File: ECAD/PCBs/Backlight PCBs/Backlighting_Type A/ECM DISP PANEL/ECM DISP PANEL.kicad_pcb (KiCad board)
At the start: 2 copper layers, 110.3 x 171.8 mm, 91 parts, among them J1 BL IN, J2 BL OUT, J3 ECM JETT, SW1 ECM JETT

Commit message: Drawing Sheet & Silkscreen update - Backlight Panels(An - Fc)
1:  Updated/Relinked Drawing Sheet for both PCB and Schematics
2:  Standardized Silkscreen (if required)
3:  Added WS2812B symbol to OH Library (for future schematic fixing)

ANT SEL thru FCS PANEL
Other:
- board text added: "ECM DISP PANEL Revision: 3 www.openhornet.com"
- board text removed: "DISP-EMC Panel Backlight Designed by L. Walker"
- board text removed: "Version 2.6"
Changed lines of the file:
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@@
   )
   (paper "A4")
+  (title_block
+    (title "ECM DISP PANEL")
+    (date "2023-02-10")
+    (rev "3")
+  )
   (layers
     (0 "F.Cu" signal)
@@
     (effects (font (size 1 1) (thickness 0.15)) (justify mirror))
   )
-  (gr_text "DISP-EMC Panel Backlight\nDesigned by L. Walker" (at 131.318 119.38) (layer "B.SilkS")
-    (effects (font (size 1 1) (thickness 0.15)) (justify left mirror))
-  )
-  (gr_text "Version 2.6" (at 87.884 117.348) (layer "B.SilkS")
+  (gr_text "ECM DISP PANEL\nRevision: 3\nwww.openhornet.com" (at 125.779172 119.871122) (layer "B.SilkS")
     (effects (font (size 1 1) (thickness 0.15)) (justify mirror))
   )

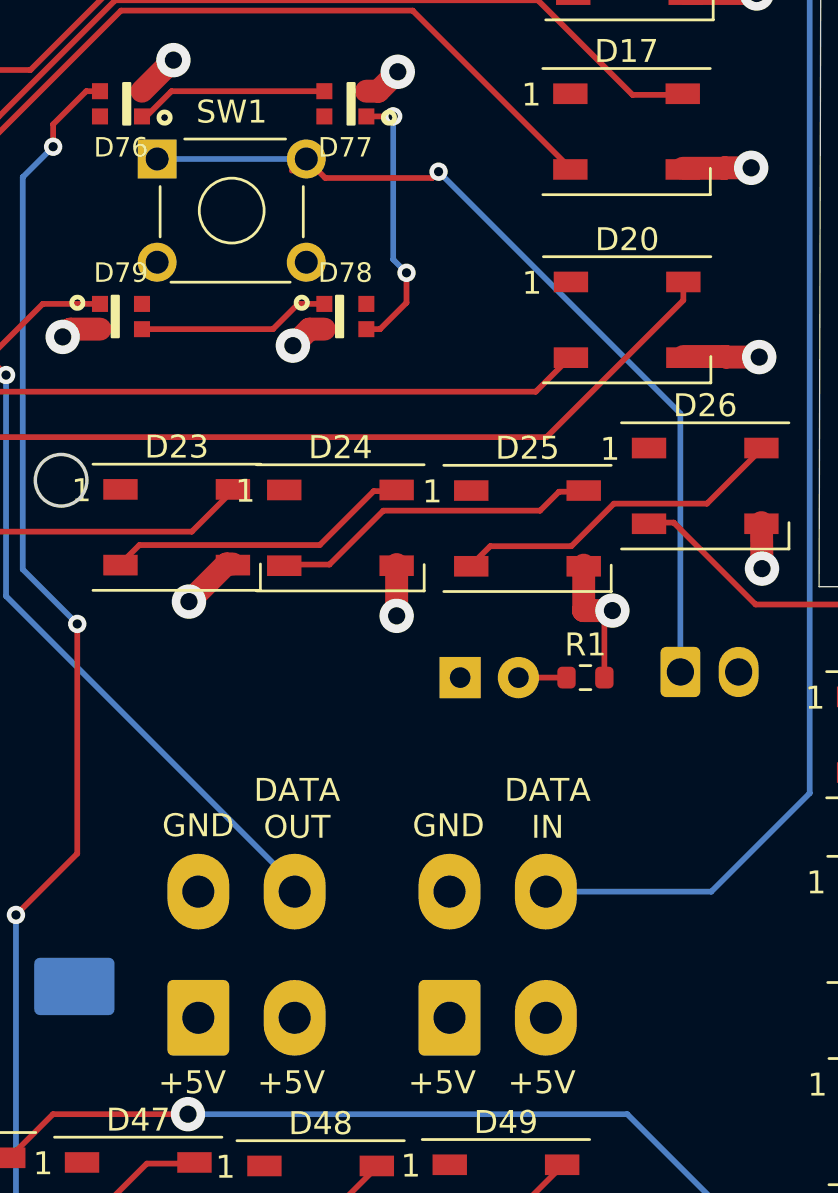
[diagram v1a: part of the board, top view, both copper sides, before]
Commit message: Review: COMM thru ECM DISP 100%
COMM PANEL
DEFOG PANEL
ECM DISP PANEL

Reviewed/adjusted silkscreens as needed
Adjusted values of footprints
Relinked footprints
Updated Manufacturing files
Updated PNGs and STEP files as needed.
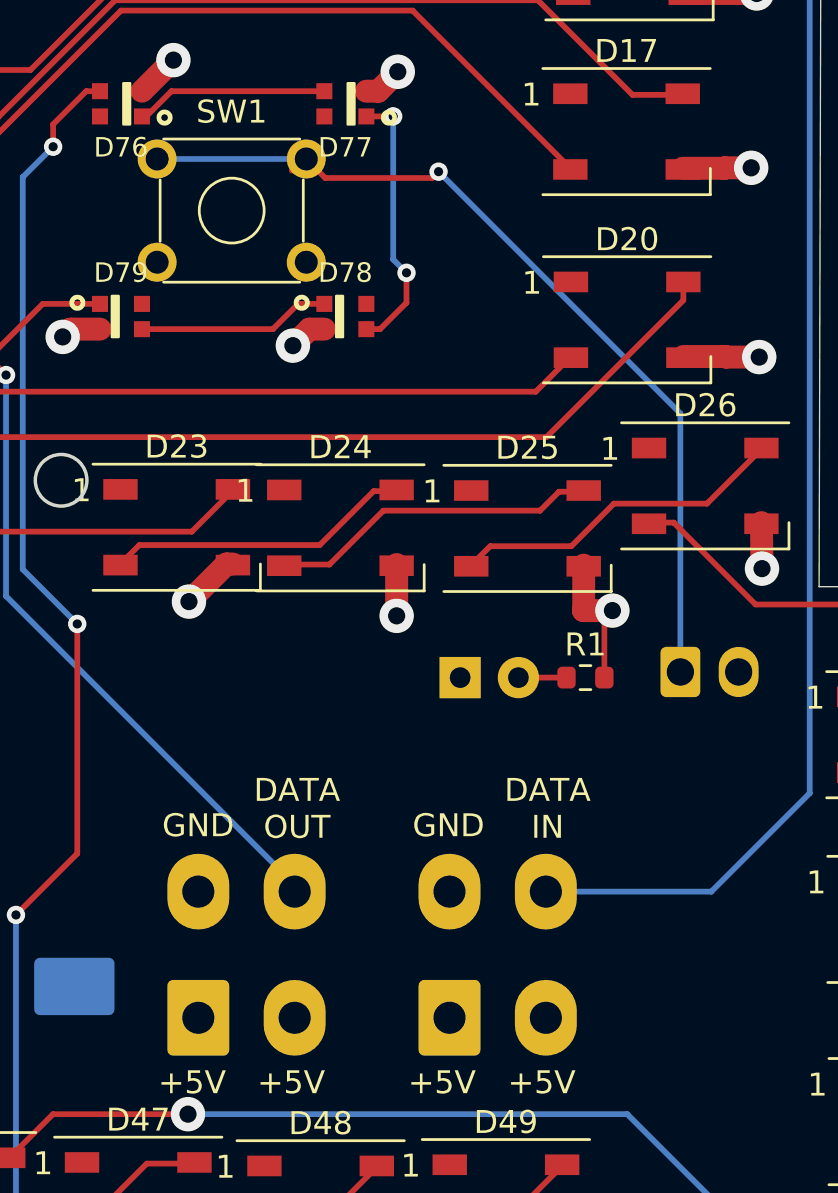
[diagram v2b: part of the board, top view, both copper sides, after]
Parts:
- C1: value 1000 nF -> 1000uF (C_Polarized)
- D1: value READY -> LED
- D76, D77, D78, D79: value LED -> REF**
- H1, H2, H3, H4, H5, H6: footprint MountingHole:MountingHole_4.5mm -> OH_Footprints:MountingHole_4.5mm
- R1: value R -> 470

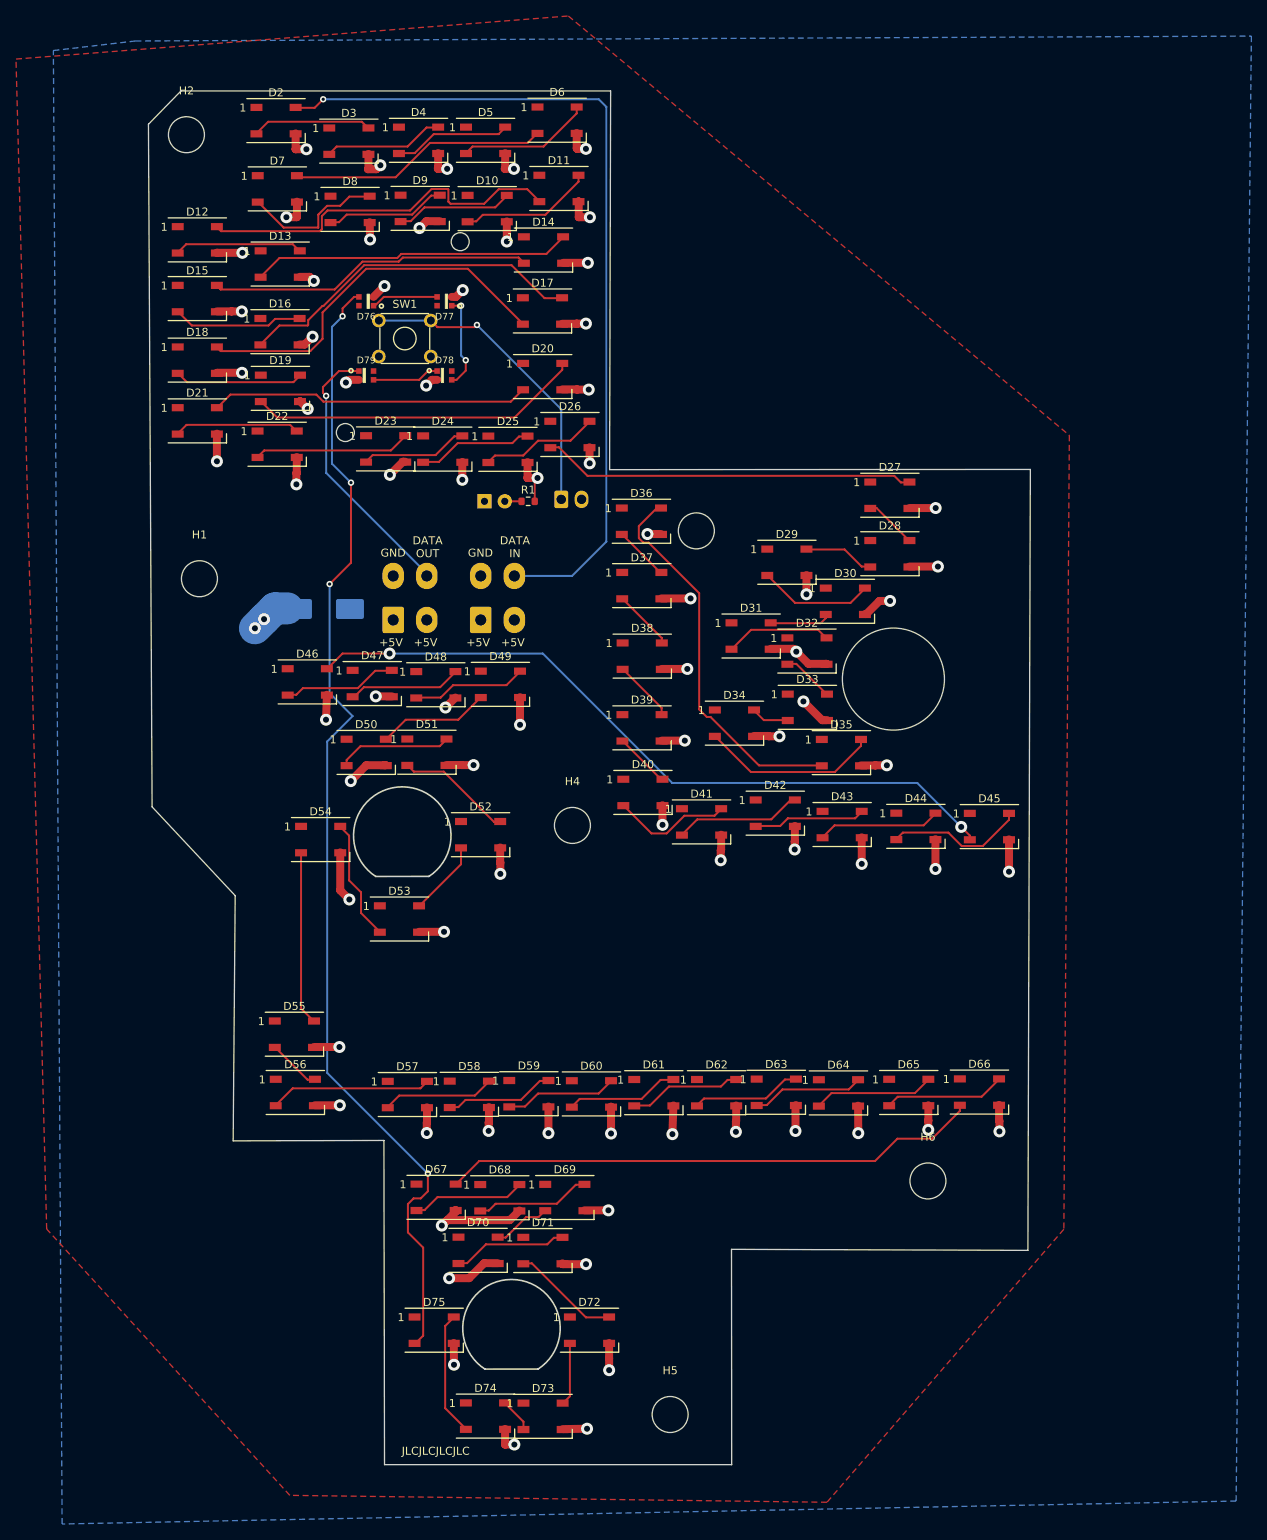
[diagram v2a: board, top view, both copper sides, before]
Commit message: Kicad 7 Transition - ECM DISP PANEL
Added 3d model and updated footprint/symbol properties for Tactical Switch, Omron B3F-1026 -
Added footprint/symbol for #0-80 mounting hole
Updated WS2818B-2020 footprint
Updated custom design rules for panels (ANT SEL thru DEFOG)

ECM DISP PANEL:
Consolidated BOM.
Updated manufacturing files
Fixed PCB routing - removed unneeded vias/traces
Fixed clearance issues around NPTHs
Updated WS2818B-2020
Schematic/PCB standardization
Updated Assets (PNGs, STEP)
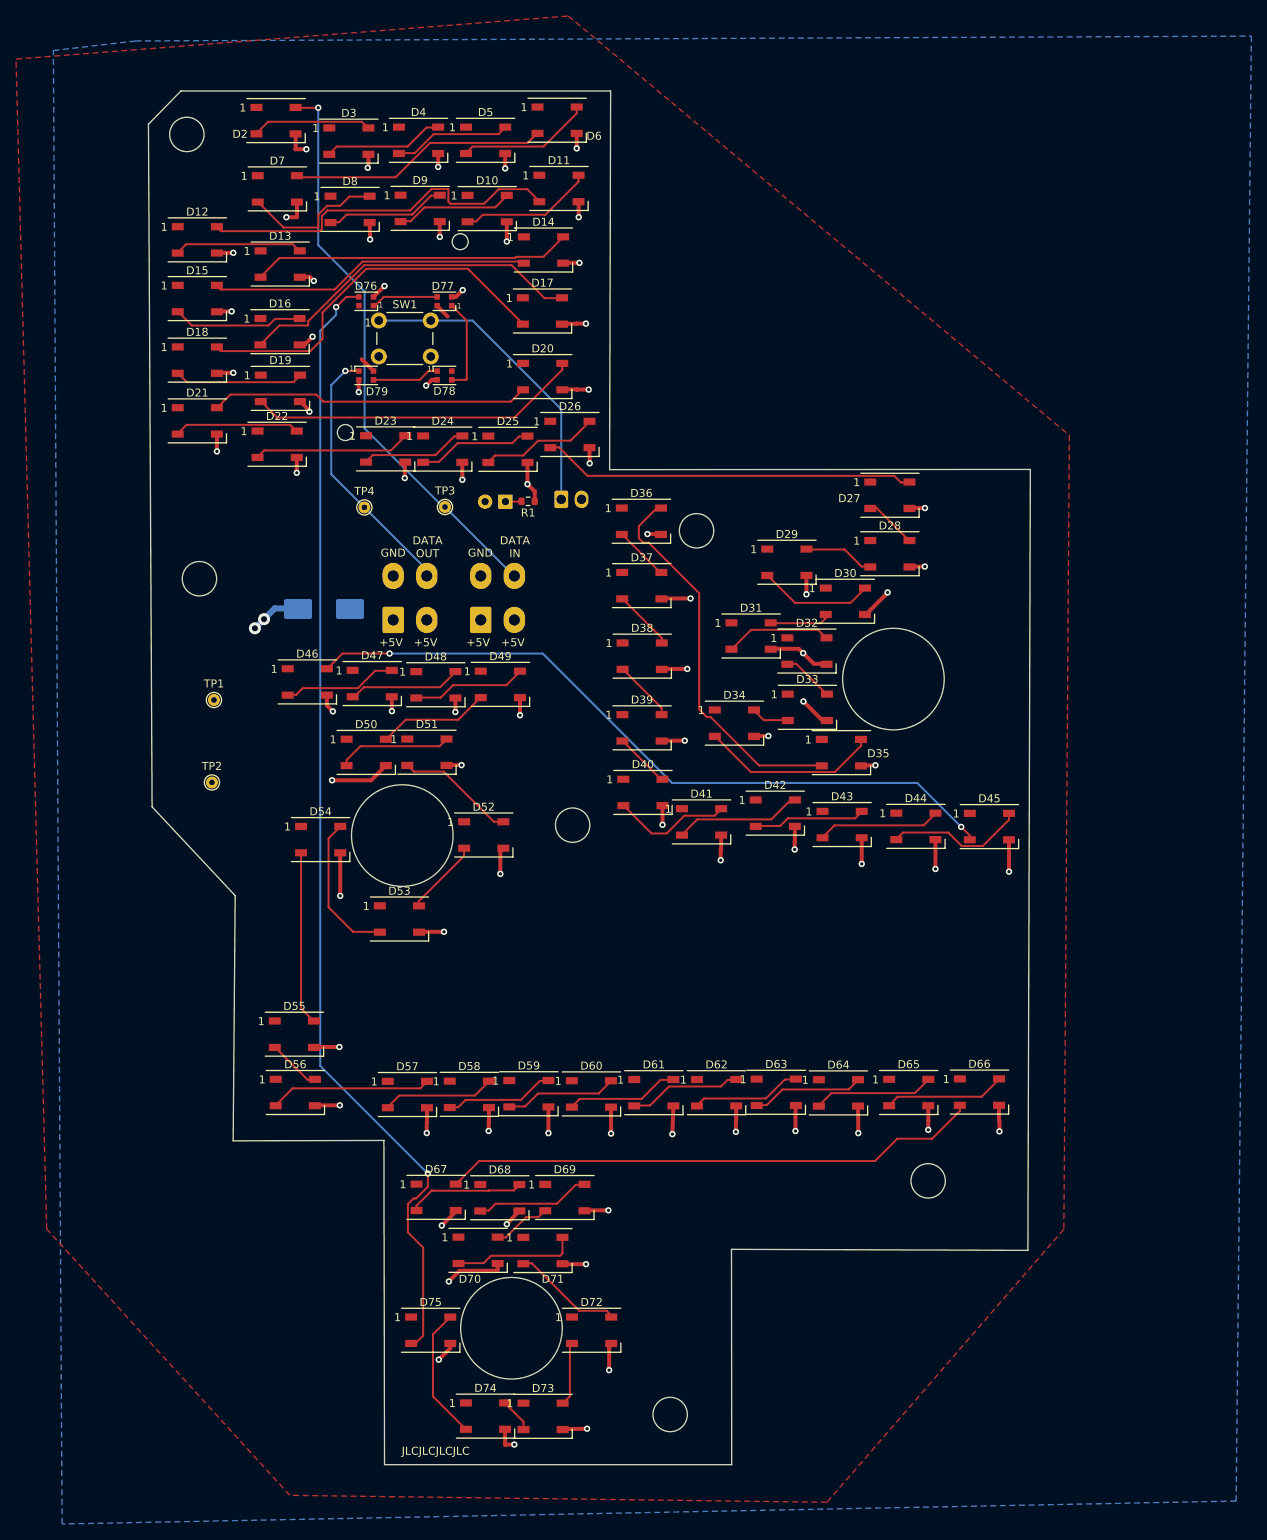
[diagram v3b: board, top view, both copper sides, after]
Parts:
- removed H1, H2, H3, H4, H5, H6: MountingHole, OH_Footprints:MountingHole_4.5mm
- added LOGO1: LOGO, OH_Footprints:LOGO_OH_Text_Large, B.Cu at (111.6, 121.6)
- added LOGO2: LOGO, OH_Footprints:LOGO_CC-BY-NC-SA_Half_Small, B.Cu at (136.1, 148.3)
- added MH1: 6x32 / 4mm, OH_Footprints:MountingHole_6-32_PHS, B.Cu at (49.4, 14.2)
- added MH10: Switch_NKK SxAL, OH_Footprints:SxAL_Toggle_13x13mm, F.Cu at (90.0, 163.5)
- added MH11: 71B36-01-2-05N, OH_Footprints:SxAL_Toggle_13x13mm, F.Cu at (137.7, 82.3)
- added MH2: 6x32 / 4mm, OH_Footprints:MountingHole_6-32_PHS, B.Cu at (113.1, 63.8)
- added MH3: 6x32 / 4mm, OH_Footprints:MountingHole_6-32_PHS, B.Cu at (51.0, 69.7)
- added MH4: 6x32 / 4mm, OH_Footprints:MountingHole_6-32_PHS, B.Cu at (97.6, 100.6)
- added MH5: 6x32 / 4mm, OH_Footprints:MountingHole_6-32_PHS, B.Cu at (142.1, 145.0)
- added MH6: 6x32 / 4mm, OH_Footprints:MountingHole_6-32_PHS, B.Cu at (109.8, 174.2)
- added MH7: #0-80/2mm, OH_Footprints:MountingHole_#0-80_2mm, B.Cu at (83.6, 27.6)
- added MH8: #0-80/2mm, OH_Footprints:MountingHole_#0-80_2mm, B.Cu at (69.2, 51.5)
- added MH9: Switch_NKK SxAL, OH_Footprints:SxAL_Toggle_13x13mm, F.Cu at (76.3, 101.9)
- added TP1: TestPoint, OH_Footprints:TestPoint_THTPad_D1.5mm_Drill0.7mm, F.Cu at (52.8, 84.9)
- added TP2: TestPoint, OH_Footprints:TestPoint_THTPad_D1.5mm_Drill0.7mm, F.Cu at (52.5, 95.2)
- added TP3: TestPoint, OH_Footprints:TestPoint_THTPad_D1.5mm_Drill0.7mm, F.Cu at (81.7, 60.8)
- added TP4: TestPoint, OH_Footprints:TestPoint_THTPad_D1.5mm_Drill0.7mm, F.Cu at (71.6, 60.8)
- C1: value 1000uF (C_Polarized) -> 1000uF
- D1: value LED -> Green
- D76, D77, D78, D79: value REF** -> WS2812B-2020; footprint OH_Footprints:WS2812-2020 -> OH_Footprints:LED_WS2812B-2020_PLCC4_2.0x2.0mm
- J1: value BL IN -> Mini-Fit Jr. 2x02
- J2: value BL OUT -> Mini-Fit Jr. 2x02
- J3: value ECM JETT -> KK-254 1x02
- SW1: value ECM JETT -> B3F-1026; footprint OH_Footprints:SW_TH_Tactile_Omron_B3F-10xx -> OH_Footprints:Omron_B3F-1026
- moved D1 2.62 mm to (89.2, 60.1), turned to 180 degrees
- moved D75 0.44 mm to (79.9, 163.7)
- moved D52 0.39 mm to (86.5, 101.8)
- moved D72 0.26 mm to (100.0, 163.7)
- turned D76 to 180 degrees
- turned D77 to 180 degrees
- turned D78 to 0 degrees
- turned D79 to 0 degrees
- turned R1 to 180 degrees
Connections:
- net /DATAIN renamed DATA IN
- net /DATAOUT renamed DATA OUT
- net Net-(D14-Pad2) renamed /DATA1
- net Net-(D27-Pad2) renamed /DATA2
- net Net-(D40-Pad2) renamed /DATA3
- net Net-(D53-Pad2) renamed /DATA4
- net Net-(D66-Pad2) renamed /DATA5
- C1 pad 1: /LED+5V -> +5V
- C1 pad 2: /LEDGND -> GND
- D1 pad 1: /LED+5V -> Net-(D1-K)
- D1 pad 2: Net-(D1-Pad2) -> +5V
- D10 pad 1: /LED+5V -> +5V
- D10 pad 3: /LEDGND -> GND
- D11 pad 1: /LED+5V -> +5V
- D11 pad 3: /LEDGND -> GND
- D12 pad 1: /LED+5V -> +5V
- D12 pad 3: /LEDGND -> GND
- D13 pad 1: /LED+5V -> +5V
- D13 pad 3: /LEDGND -> GND
- D14 pad 1: /LED+5V -> +5V
- D14 pad 3: /LEDGND -> GND
- D15 pad 1: /LED+5V -> +5V
- D15 pad 3: /LEDGND -> GND
- D16 pad 1: /LED+5V -> +5V
- D16 pad 3: /LEDGND -> GND
- D17 pad 1: /LED+5V -> +5V
- D17 pad 3: /LEDGND -> GND
- D18 pad 1: /LED+5V -> +5V
- D18 pad 3: /LEDGND -> GND
- D19 pad 1: /LED+5V -> +5V
- D19 pad 3: /LEDGND -> GND
- D2 pad 1: /LED+5V -> +5V
- D2 pad 3: /LEDGND -> GND
- D20 pad 1: /LED+5V -> +5V
- D20 pad 3: /LEDGND -> GND
- D21 pad 1: /LED+5V -> +5V
- D21 pad 3: /LEDGND -> GND
- D22 pad 1: /LED+5V -> +5V
- D22 pad 3: /LEDGND -> GND
- D23 pad 1: /LED+5V -> +5V
- D23 pad 3: /LEDGND -> GND
- D24 pad 1: /LED+5V -> +5V
- D24 pad 3: /LEDGND -> GND
- D25 pad 1: /LED+5V -> +5V
- D25 pad 3: /LEDGND -> GND
- D26 pad 1: /LED+5V -> +5V
- D26 pad 3: /LEDGND -> GND
- D27 pad 1: /LED+5V -> +5V
- D27 pad 3: /LEDGND -> GND
- D28 pad 1: /LED+5V -> +5V
- D28 pad 3: /LEDGND -> GND
- D29 pad 1: /LED+5V -> +5V
- D29 pad 3: /LEDGND -> GND
- D3 pad 1: /LED+5V -> +5V
- D3 pad 3: /LEDGND -> GND
- D30 pad 1: /LED+5V -> +5V
- D30 pad 3: /LEDGND -> GND
- D31 pad 1: /LED+5V -> +5V
- D31 pad 3: /LEDGND -> GND
- D32 pad 1: /LED+5V -> +5V
- D32 pad 3: /LEDGND -> GND
- D33 pad 1: /LED+5V -> +5V
- D33 pad 3: /LEDGND -> GND
- D34 pad 1: /LED+5V -> +5V
- D34 pad 3: /LEDGND -> GND
- D35 pad 1: /LED+5V -> +5V
- D35 pad 3: /LEDGND -> GND
- D36 pad 1: /LED+5V -> +5V
- D36 pad 3: /LEDGND -> GND
- D37 pad 1: /LED+5V -> +5V
- D37 pad 3: /LEDGND -> GND
- D38 pad 1: /LED+5V -> +5V
- D38 pad 3: /LEDGND -> GND
- D39 pad 1: /LED+5V -> +5V
- D39 pad 3: /LEDGND -> GND
- D4 pad 1: /LED+5V -> +5V
- D4 pad 3: /LEDGND -> GND
- D40 pad 1: /LED+5V -> +5V
- D40 pad 3: /LEDGND -> GND
- D41 pad 1: /LED+5V -> +5V
- D41 pad 3: /LEDGND -> GND
- D42 pad 1: /LED+5V -> +5V
- D42 pad 3: /LEDGND -> GND
- D43 pad 1: /LED+5V -> +5V
- D43 pad 3: /LEDGND -> GND
- D44 pad 1: /LED+5V -> +5V
- D44 pad 3: /LEDGND -> GND
- D45 pad 1: /LED+5V -> +5V
- D45 pad 3: /LEDGND -> GND
- D46 pad 1: /LED+5V -> +5V
- D46 pad 3: /LEDGND -> GND
- D47 pad 1: /LED+5V -> +5V
- D47 pad 3: /LEDGND -> GND
- D48 pad 1: /LED+5V -> +5V
- D48 pad 3: /LEDGND -> GND
- D49 pad 1: /LED+5V -> +5V
- D49 pad 3: /LEDGND -> GND
- D5 pad 1: /LED+5V -> +5V
- D5 pad 3: /LEDGND -> GND
- D50 pad 1: /LED+5V -> +5V
- D50 pad 3: /LEDGND -> GND
- D51 pad 1: /LED+5V -> +5V
- D51 pad 3: /LEDGND -> GND
- D52 pad 1: /LED+5V -> +5V
- D52 pad 3: /LEDGND -> GND
- D53 pad 1: /LED+5V -> +5V
- D53 pad 3: /LEDGND -> GND
- D54 pad 1: /LED+5V -> +5V
- D54 pad 3: /LEDGND -> GND
- D55 pad 1: /LED+5V -> +5V
- D55 pad 3: /LEDGND -> GND
- D56 pad 1: /LED+5V -> +5V
- D56 pad 3: /LEDGND -> GND
- D57 pad 1: /LED+5V -> +5V
- D57 pad 3: /LEDGND -> GND
- D58 pad 1: /LED+5V -> +5V
- D58 pad 3: /LEDGND -> GND
- D59 pad 1: /LED+5V -> +5V
- D59 pad 3: /LEDGND -> GND
- D6 pad 1: /LED+5V -> +5V
- D6 pad 3: /LEDGND -> GND
- D60 pad 1: /LED+5V -> +5V
- D60 pad 3: /LEDGND -> GND
- D61 pad 1: /LED+5V -> +5V
- D61 pad 3: /LEDGND -> GND
- D62 pad 1: /LED+5V -> +5V
- D62 pad 3: /LEDGND -> GND
- D63 pad 1: /LED+5V -> +5V
- D63 pad 3: /LEDGND -> GND
- D64 pad 1: /LED+5V -> +5V
- D64 pad 3: /LEDGND -> GND
- D65 pad 1: /LED+5V -> +5V
- D65 pad 3: /LEDGND -> GND
- D66 pad 1: /LED+5V -> +5V
- D66 pad 3: /LEDGND -> GND
- D67 pad 1: /LED+5V -> +5V
- D67 pad 3: /LEDGND -> GND
- D68 pad 1: /LED+5V -> +5V
- D68 pad 3: /LEDGND -> GND
- D69 pad 1: /LED+5V -> +5V
- D69 pad 3: /LEDGND -> GND
- D7 pad 1: /LED+5V -> +5V
- D7 pad 3: /LEDGND -> GND
- D70 pad 1: /LED+5V -> +5V
- D70 pad 3: /LEDGND -> GND
- D71 pad 1: /LED+5V -> +5V
- D71 pad 3: /LEDGND -> GND
- D72 pad 1: /LED+5V -> +5V
- D72 pad 3: /LEDGND -> GND
- D73 pad 1: /LED+5V -> +5V
- D73 pad 3: /LEDGND -> GND
- D74 pad 1: /LED+5V -> +5V
- D74 pad 3: /LEDGND -> GND
- D75 pad 1: /LED+5V -> +5V
- D75 pad 3: /LEDGND -> GND
- D76 pad 2: /LEDGND -> GND
- D76 pad 4: /LED+5V -> +5V
- D77 pad 2: /LEDGND -> GND
- D77 pad 4: /LED+5V -> +5V
- D78 pad 2: /LEDGND -> GND
- D78 pad 4: /LED+5V -> +5V
- D79 pad 2: /LEDGND -> GND
- D79 pad 4: /LED+5V -> +5V
- D8 pad 1: /LED+5V -> +5V
- D8 pad 3: /LEDGND -> GND
- D9 pad 1: /LED+5V -> +5V
- D9 pad 3: /LEDGND -> GND
- J1 pad 1: /LED+5V -> +5V
- J1 pad 2: /LED+5V -> +5V
- J1 pad 3: /LEDGND -> GND
- J2 pad 1: /LED+5V -> +5V
- J2 pad 2: /LED+5V -> +5V
- J2 pad 3: /LEDGND -> GND
- J3 pad 2: /LEDGND -> GND
- R1 pad 1: Net-(D1-Pad2) -> GND
- R1 pad 2: /LEDGND -> Net-(D1-K)
- SW1 pad 3: (no net) -> GND
- SW1 pad 4: (no net) -> GND
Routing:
- net /LEDGND: track 254.8 -> 0.00 mm, vias 76 -> 0
- net GND: track 0.00 -> 220.5 mm, vias 0 -> 77
- net DATA IN: track 107.3 -> 71.4 mm
- net +5V: track 0.00 -> 9.07 mm, vias 0 -> 2
- net /LED+5V: track 5.11 -> 0.00 mm, vias 2 -> 0
- net Net-(D75-DOUT): track 145.2 -> 141.7 mm, vias 4 -> 2
- net /DATA4: track 15.2 -> 18.4 mm
- net Net-(D1-Pad2): track 2.10 -> 0.00 mm
- net DATA OUT: track 34.3 -> 32.2 mm
- net Net-(D1-K): track 0.00 -> 1.98 mm
- net /SW_JETT: track 40.2 -> 38.7 mm, vias 1 -> 0
- net Net-(D74-DOUT): track 15.5 -> 16.6 mm
- net Net-(D70-DOUT): track 14.3 -> 15.5 mm
- net /DATA1: track 40.5 -> 39.9 mm
- net Net-(D41-DOUT): track 15.9 -> 15.3 mm
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- added copper zone on F.Cu, net +5V
- added copper zone on B.Cu, net GND
- removed copper zone on F.Cu, net /LED+5V
- removed copper zone on B.Cu, net /LEDGND
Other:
- outline, holes or cut-outs redrawn
- board text added: "0.2000 mm"
- board text added: "0.2000 mm / 0.1270 mm"
- board text added: "1"
- board text added: "1.6000 mm"
- board text added: "110.2614 mm x 171.7548 mm"
- board text added: "2"
- board text added: "BOARD CHARACTERISTICS"
- board text added: "Board Thickness:"
- board text added: "Board overall dimensions:"
- board text added: "Castellated pads:"
- board text added: "Copper Finish:"
- board text added: "Copper Layer Count:"
- board text added: "DISPENSER"
- board text added: "ECM DISP PANEL REV: 4 WWW.OPENHORNET.COM"
- board text added: "ECM JETT CONN."
- board text added: "ECM JETT SWITCH"
- board text added: "Edge card connectors:"
- board text added: "Impedance Control:"
- board text added: "Min hole diameter:"
- board text added: "Min track/spacing:"
- board text added: "No"
- board text added: "None"
- board text added: "POWER REQUIREMENTS: VOLTAGE: 5V DC LEDS: 78 CURRENT: 4.7A WATTAGE: 23.5W"
- board text added: "Plated Board Edge:"
- board text removed: "DESPENSER"
- board text removed: "ECM DISP PANEL Revision: 3 www.openhornet.com"
- board text removed: "ECM JETT"
- board text removed: "ECM JETT BUTTON"
- board text removed: "POWER REQUIREMENTS: VOLTAGE: 5V DC LEDS: 58 CURRENT: 3.48A WATTAGE: 17.4W"
